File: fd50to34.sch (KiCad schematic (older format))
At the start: 9 parts, among them J1 FD50, J2 FD34

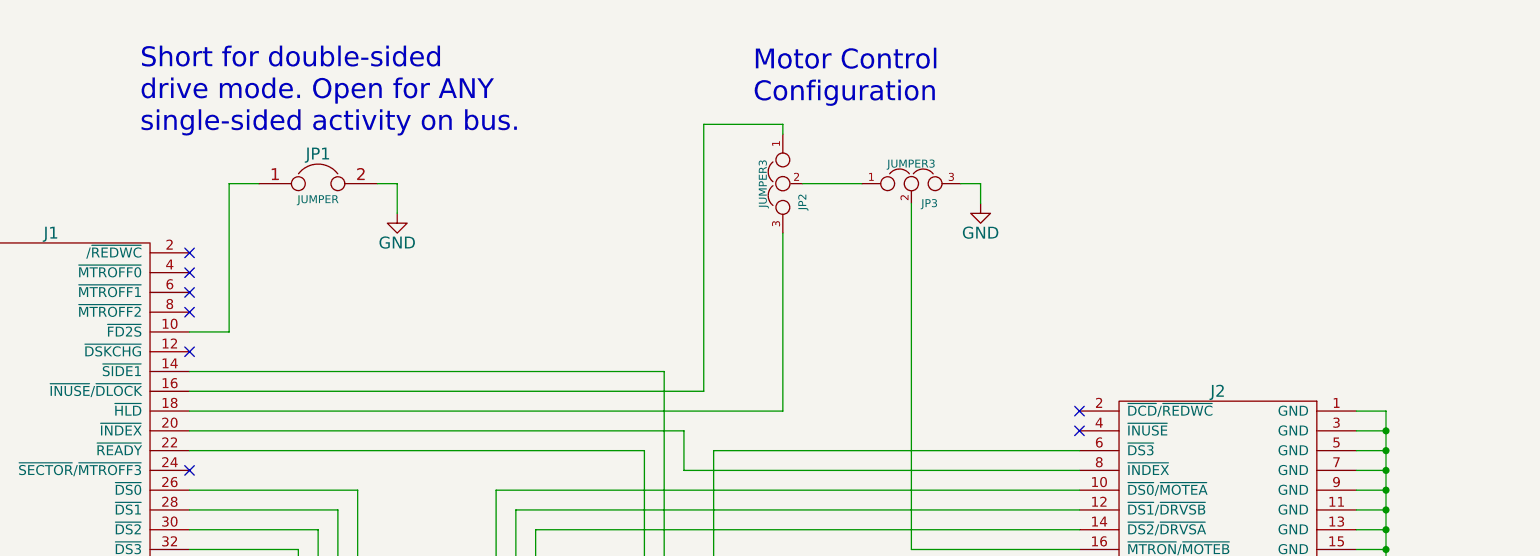
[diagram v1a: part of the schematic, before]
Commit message: Added density select jumper.
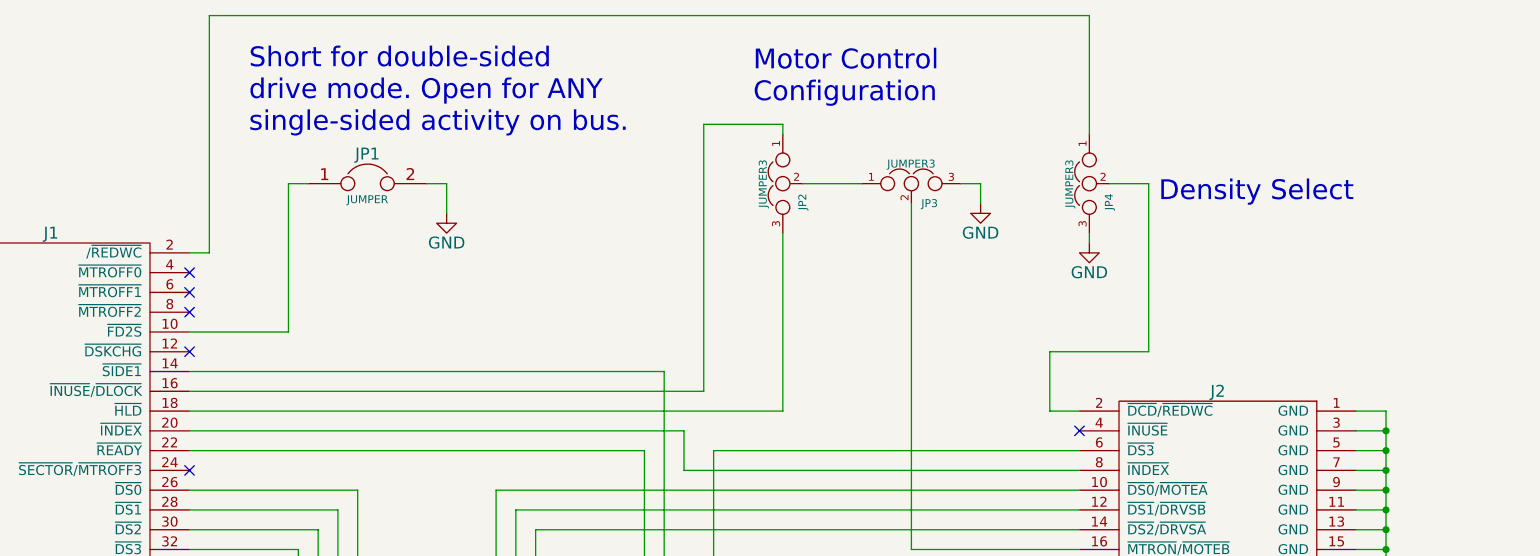
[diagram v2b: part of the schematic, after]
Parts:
- added JP4: JUMPER3, Pin_Headers:Pin_Header_Angled_1x03, symbol JUMPER3
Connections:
- net GND: now also JP4.3
- net at J1.2 (/~REDWC): now also JP4.1
- net at J2.2 (~DCD~/~REDWC): now also JP4.2
- no-connect marks 10 -> 8
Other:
- note added: "Density Select"
- moved on the sheet: JP1
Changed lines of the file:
@@
 Sheet 1 1
 Title "fd50to34: Adapt 34 pin floppy drives to 50 pin controllers"
-Date "2015-07-05"
-Rev "2.0-DRAFT"
+Date "2015-07-30"
+Rev "2.0"
 Comp "Mark J. Blair <nf6x@nf6x.net>"
 Comment1 "https://github.com/NF6X/fd50to34"
@@
 NoConn ~ 3250 3600
 NoConn ~ 7750 3400
-NoConn ~ 7750 3300
 NoConn ~ 3250 3000
-NoConn ~ 3250 2500
 $Comp
 L JUMPER JP1
 U 1 1 5599D454
-P 3900 2150
-F 0 "JP1" H 3900 2300 60  0000 C CNN
-F 1 "JUMPER" H 3900 2070 40  0000 C CNN
-F 2 "Pin_Headers:Pin_Header_Angled_1x02" H 3900 2150 60  0001 C CNN
-F 3 "" H 3900 2150 60  0000 C CNN
-	1    3900 2150
+P 4150 2150
+F 0 "JP1" H 4150 2300 60  0000 C CNN
+F 1 "JUMPER" H 4150 2070 40  0000 C CNN
+F 2 "Pin_Headers:Pin_Header_Angled_1x02" H 4150 2150 60  0001 C CNN
+F 3 "" H 4150 2150 60  0000 C CNN
+	1    4150 2150
 	1    0    0    -1
 $EndComp
@@
 L GND #PWR03
 U 1 1 5599D494
-P 4300 2300
-F 0 "#PWR03" H 4300 2050 60  0001 C CNN
-F 1 "GND" H 4300 2150 60  0000 C CNN
-F 2 "" H 4300 2300 60  0000 C CNN
-F 3 "" H 4300 2300 60  0000 C CNN
-	1    4300 2300
+P 4550 2300
+F 0 "#PWR03" H 4550 2050 60  0001 C CNN
+F 1 "GND" H 4550 2150 60  0000 C CNN
+F 2 "" H 4550 2300 60  0000 C CNN
+F 3 "" H 4550 2300 60  0000 C CNN
+	1    4550 2300
 	1    0    0    -1
 $EndComp
@@
 Text Notes 7500 5500 0    100  ~ 0
 3.5"/5.25" Floppy Drive(s)
-Text Notes 3000 1900 0    100  ~ 0
+Text Notes 3550 1900 0    100  ~ 0
 Short for double-sided\ndrive mode. Open for ANY\nsingle-sided activity on bus.
 Text Notes 6100 1750 0    100  ~ 0
@@
 	5550 4900 7750 4900
 Wire Wire Line
-	3250 2900 3450 2900
-Wire Wire Line
-	3450 2900 3450 2150
-Wire Wire Line
-	3450 2150 3600 2150
-Wire Wire Line
-	4200 2150 4300 2150
-Wire Wire Line
-	4300 2150 4300 2300
+	4450 2150 4550 2150
+Wire Wire Line
+	4550 2150 4550 2300
 Wire Wire Line
 	6900 2250 6900 4000
@@
 Wire Notes Line
 	3650 4850 5150 4850
+$Comp
+L JUMPER3 JP4
+U 1 1 55BA433A
+P 7800 2150
+F 0 "JP4" H 7850 2050 40  0000 L CNN
+F 1 "JUMPER3" H 7800 2250 40  0000 C CNN
+F 2 "Pin_Headers:Pin_Header_Angled_1x03" H 7800 2150 60  0001 C CNN
+F 3 "" H 7800 2150 60  0000 C CNN
+	1    7800 2150
+	0    -1   1    0
+$EndComp
+$Comp
+L GND #PWR05
+U 1 1 55BA44B8
+P 7800 2450
+F 0 "#PWR05" H 7800 2200 60  0001 C CNN
+F 1 "GND" H 7800 2300 60  0000 C CNN
+F 2 "" H 7800 2450 60  0000 C CNN
+F 3 "" H 7800 2450 60  0000 C CNN
+	1    7800 2450
+	1    0    0    -1
+$EndComp
+Wire Wire Line
+	7750 3300 7600 3300
+Wire Wire Line
+	7600 3300 7600 3000
+Wire Wire Line
+	7600 3000 8100 3000
+Wire Wire Line
+	8100 3000 8100 2150
+Wire Wire Line
+	8100 2150 7900 2150
+Wire Wire Line
+	7800 2400 7800 2450
+Wire Wire Line
+	3250 2900 3750 2900
+Wire Wire Line
+	3750 2900 3750 2150
+Wire Wire Line
+	3750 2150 3850 2150
+Wire Wire Line
+	3250 2500 3350 2500
+Wire Wire Line
+	3350 2500 3350 1300
+Wire Wire Line
+	3350 1300 7800 1300
+Wire Wire Line
+	7800 1300 7800 1900
+Text Notes 8150 2250 0    100  ~ 0
+Density Select
 $EndSCHEMATC

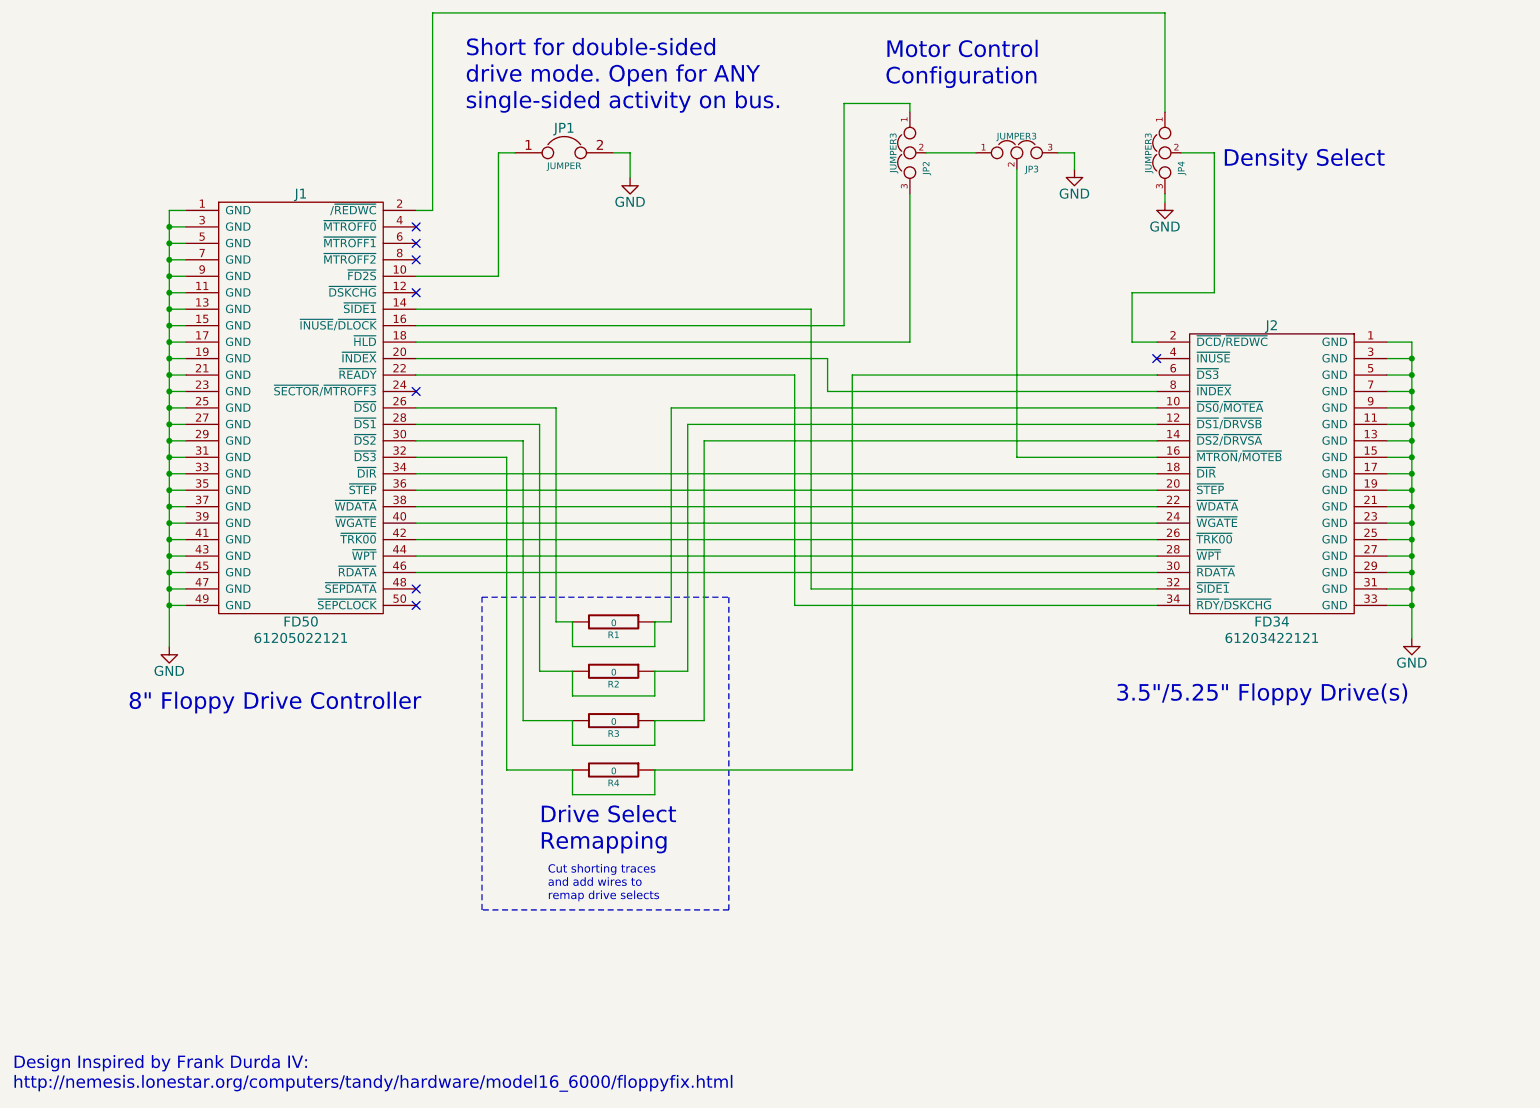
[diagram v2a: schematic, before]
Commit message: Revised part numbers for production quote at MacroFab.
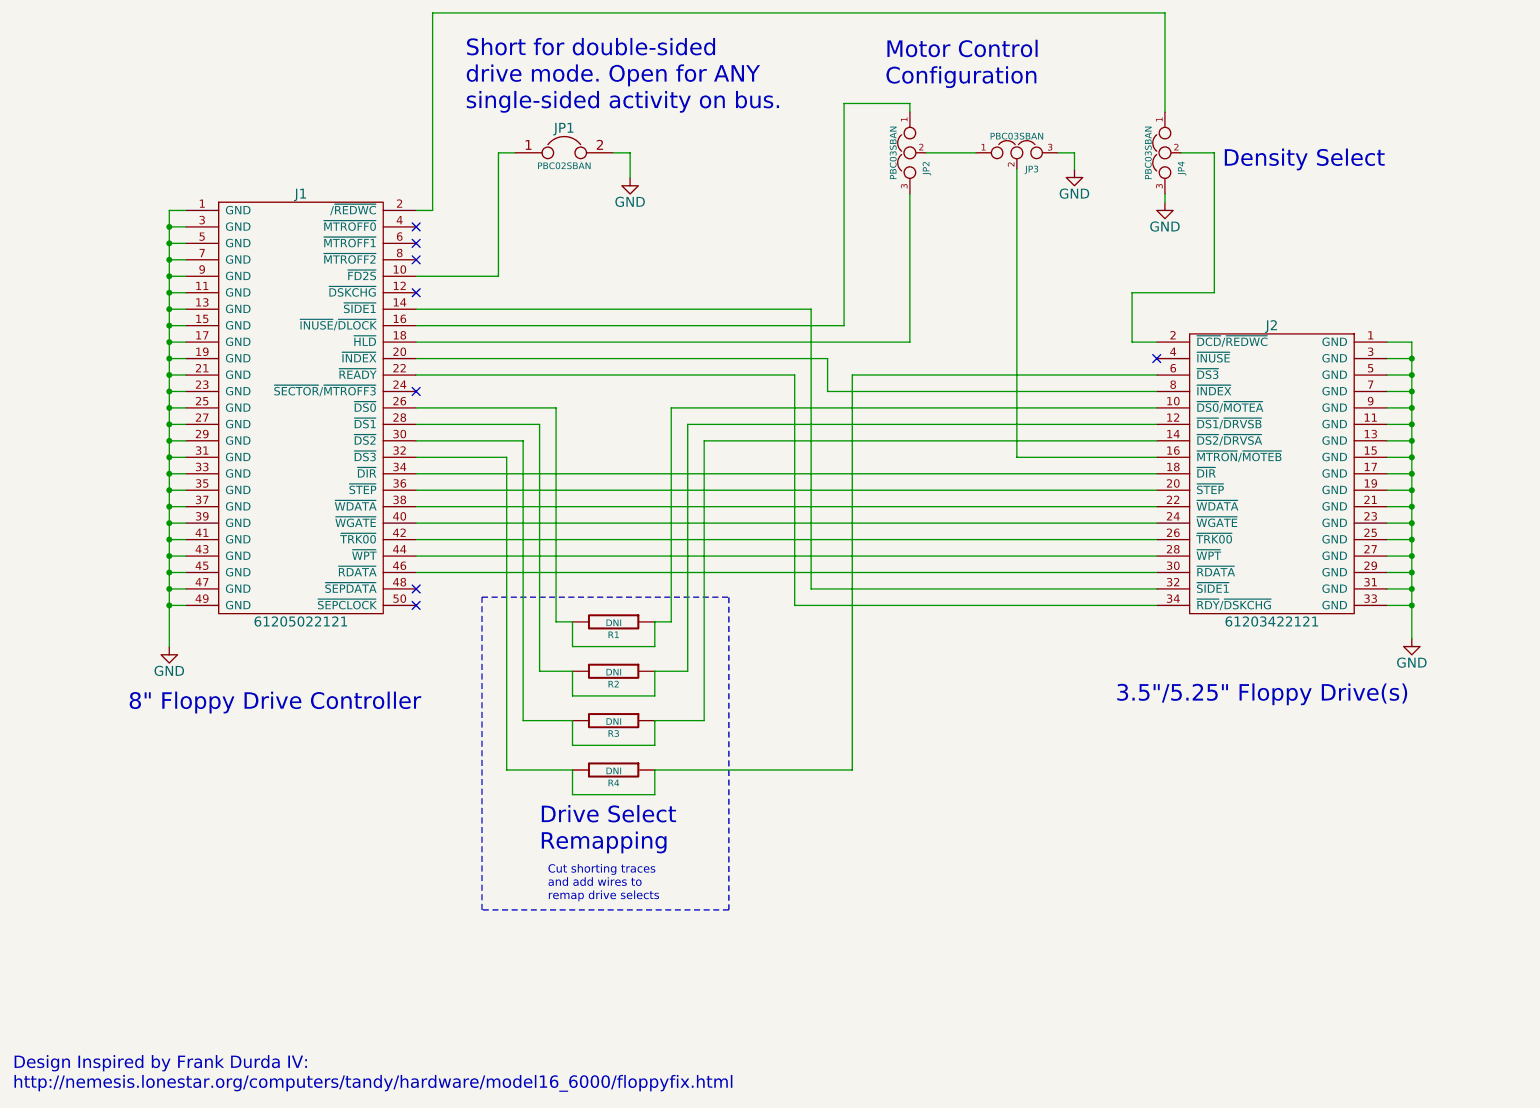
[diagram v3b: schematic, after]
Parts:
- J1: value FD50 -> 61205022121
- J2: value FD34 -> 61203422121
- JP1: value JUMPER -> PBC02SBAN
- JP2, JP3, JP4: value JUMPER3 -> PBC03SBAN
- R1, R2, R3, R4: value 0 -> DNI
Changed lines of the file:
@@
 Sheet 1 1
 Title "fd50to34: Adapt 34 pin floppy drives to 50 pin controllers"
-Date "2015-07-30"
-Rev "2.0"
+Date "2015-08-19"
+Rev "2.1"
 Comp "Mark J. Blair <nf6x@nf6x.net>"
 Comment1 "https://github.com/NF6X/fd50to34"
@@
 P 2550 3700
 F 0 "J1" H 2550 5000 60  0000 C CNN
-F 1 "FD50" H 2550 2400 60  0000 C CNN
+F 1 "61205022121" H 2550 2400 60  0000 C CNN
 F 2 "NF6X_Connectors:Wurth_61205022121" H 2550 2200 60  0001 C CNN
 F 3 "" H 2300 4150 60  0000 C CNN
-F 4 "61205022121" H 2550 2300 60  0000 C CNN "PartNum"
+F 4 "61205022121" H 2550 2300 60  0001 C CNN "PartNum"
 	1    2550 3700
 	1    0    0    -1
@@
 P 8450 4100
 F 0 "J2" H 8450 5000 60  0000 C CNN
-F 1 "FD34" H 8450 3200 60  0000 C CNN
+F 1 "61203422121" H 8450 3200 60  0000 C CNN
 F 2 "NF6X_Connectors:Wurth_61203422121" H 8450 3000 60  0001 C CNN
 F 3 "" H 8200 4150 60  0000 C CNN
-F 4 "61203422121" H 8450 3100 60  0000 C CNN "PartNum"
+F 4 "61203422121" H 8450 3100 60  0001 C CNN "PartNum"
 	1    8450 4100
 	-1   0    0    -1
@@
 P 4150 2150
 F 0 "JP1" H 4150 2300 60  0000 C CNN
-F 1 "JUMPER" H 4150 2070 40  0000 C CNN
+F 1 "PBC02SBAN" H 4150 2070 40  0000 C CNN
 F 2 "Pin_Headers:Pin_Header_Angled_1x02" H 4150 2150 60  0001 C CNN
 F 3 "" H 4150 2150 60  0000 C CNN
@@
 P 6900 2150
 F 0 "JP3" H 6950 2050 40  0000 L CNN
-F 1 "JUMPER3" H 6900 2250 40  0000 C CNN
+F 1 "PBC03SBAN" H 6900 2250 40  0000 C CNN
 F 2 "Pin_Headers:Pin_Header_Angled_1x03" H 6900 2150 60  0001 C CNN
 F 3 "" H 6900 2150 60  0000 C CNN
@@
 P 6250 2150
 F 0 "JP2" H 6300 2050 40  0000 L CNN
-F 1 "JUMPER3" H 6250 2250 40  0000 C CNN
+F 1 "PBC03SBAN" H 6250 2250 40  0000 C CNN
 F 2 "Pin_Headers:Pin_Header_Angled_1x03" H 6250 2150 60  0001 C CNN
 F 3 "" H 6250 2150 60  0000 C CNN
@@
 P 4450 5000
 F 0 "R1" V 4530 5000 40  0000 C CNN
-F 1 "0" V 4457 5001 40  0000 C CNN
+F 1 "DNI" V 4457 5001 40  0000 C CNN
 F 2 "Resistors_ThroughHole:Resistor_Horizontal_RM10mm" V 4380 5000 30  0001 C CNN
 F 3 "" H 4450 5000 30  0000 C CNN
@@
 P 4450 5300
 F 0 "R2" V 4530 5300 40  0000 C CNN
-F 1 "0" V 4457 5301 40  0000 C CNN
+F 1 "DNI" V 4457 5301 40  0000 C CNN
 F 2 "Resistors_ThroughHole:Resistor_Horizontal_RM10mm" V 4380 5300 30  0001 C CNN
 F 3 "" H 4450 5300 30  0000 C CNN
@@
 P 4450 5600
 F 0 "R3" V 4530 5600 40  0000 C CNN
-F 1 "0" V 4457 5601 40  0000 C CNN
+F 1 "DNI" V 4457 5601 40  0000 C CNN
 F 2 "Resistors_ThroughHole:Resistor_Horizontal_RM10mm" V 4380 5600 30  0001 C CNN
 F 3 "" H 4450 5600 30  0000 C CNN
@@
 P 4450 5900
 F 0 "R4" V 4530 5900 40  0000 C CNN
-F 1 "0" V 4457 5901 40  0000 C CNN
+F 1 "DNI" V 4457 5901 40  0000 C CNN
 F 2 "Resistors_ThroughHole:Resistor_Horizontal_RM10mm" V 4380 5900 30  0001 C CNN
 F 3 "" H 4450 5900 30  0000 C CNN
@@
 P 7800 2150
 F 0 "JP4" H 7850 2050 40  0000 L CNN
-F 1 "JUMPER3" H 7800 2250 40  0000 C CNN
+F 1 "PBC03SBAN" H 7800 2250 40  0000 C CNN
 F 2 "Pin_Headers:Pin_Header_Angled_1x03" H 7800 2150 60  0001 C CNN
 F 3 "" H 7800 2150 60  0000 C CNN
